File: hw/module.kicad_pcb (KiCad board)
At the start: 2 copper layers, 30 x 30 mm, 42 parts, among them Q1 MUN 2211, U1 CFPS-39, U2 CFPS-39, U3 74LVC1G125, U4 74 LVC 1G3157GW,125, U5 MAX919, U6 STM32L010F4P6, U7 BAS70-7-F, U8 SS39ET

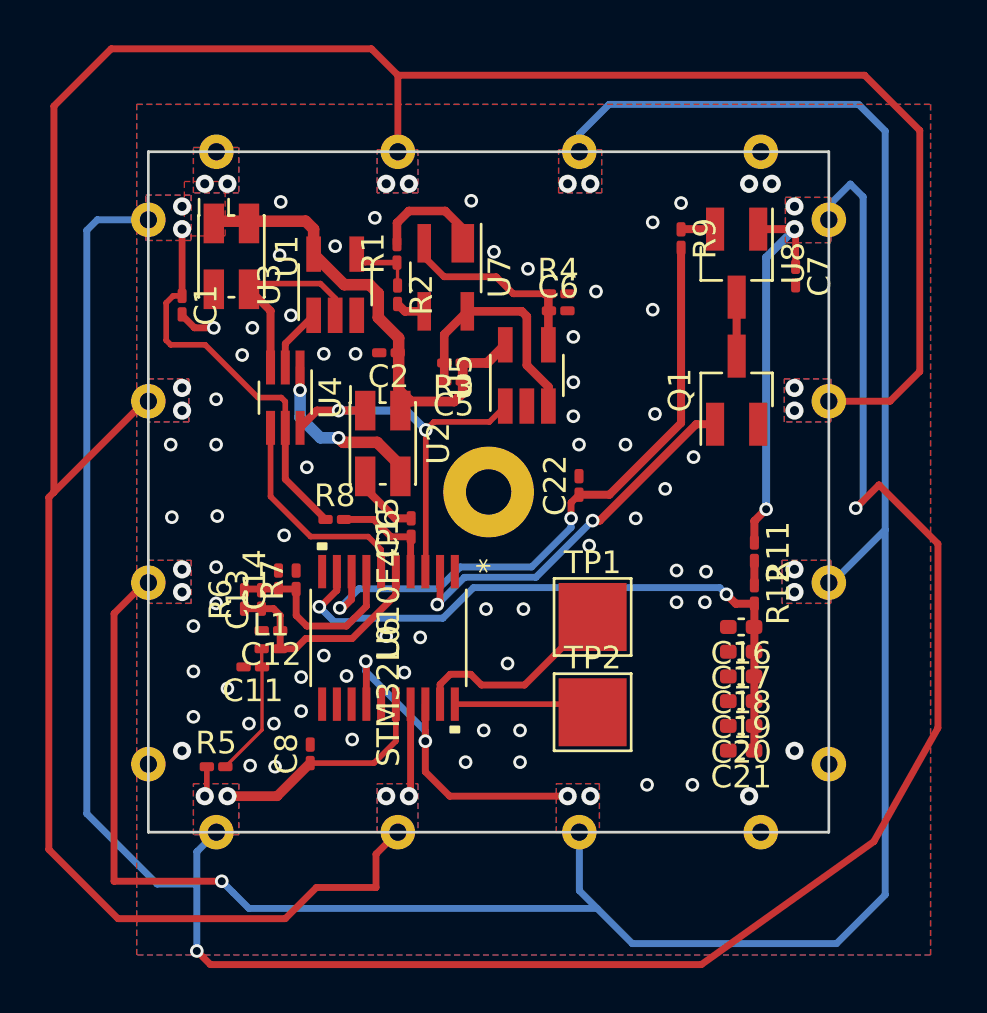
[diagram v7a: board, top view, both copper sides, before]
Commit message: Add extra resistor for capacitor measure, remove out-the-board wires
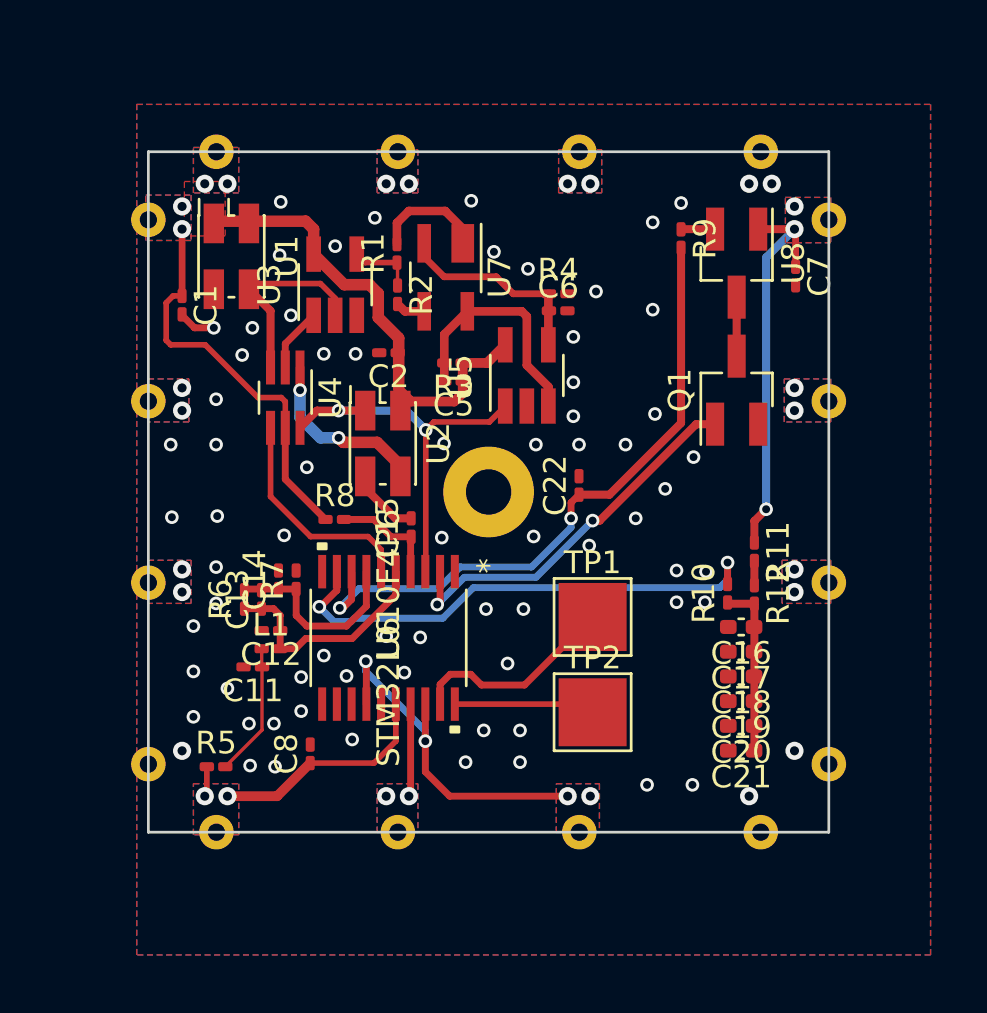
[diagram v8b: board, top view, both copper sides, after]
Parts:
- added R10: 150k, Resistor_SMD:R_0201_0603Metric_Pad0.64x0.40mm_HandSolder, F.Cu at (68.5, 61.5)
- C22: value 200p -> 100n
- C8: value 100n -> 10n
- R9: value 100 -> 10k
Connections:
- C16 pad 1: /Cap_experiment -> Net-(C16-Pad1)
- C17 pad 1: /Cap_experiment -> Net-(C16-Pad1)
- C18 pad 1: /Cap_experiment -> Net-(C16-Pad1)
- C19 pad 1: /Cap_experiment -> Net-(C16-Pad1)
- C20 pad 1: /Cap_experiment -> Net-(C16-Pad1)
- C21 pad 1: /Cap_experiment -> Net-(C16-Pad1)
- R12 pad 2: /Cap_experiment -> Net-(C16-Pad1)
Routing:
- net /TX: track 120.6 -> 4.09 mm
- net +3.3V: track 175.2 -> 67.7 mm, vias 11 -> 9
- net /RX: track 121.6 -> 16.2 mm, vias 11 -> 10
- net Net-(C16-Pad1): track 0.00 -> 7.69 mm
- net /Cap_experiment: track 28.7 -> 22.6 mm
- net GND: vias 70 -> 74
